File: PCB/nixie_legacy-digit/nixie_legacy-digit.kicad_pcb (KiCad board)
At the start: 2 copper layers, 50.8 x 78.7 mm, 11 parts

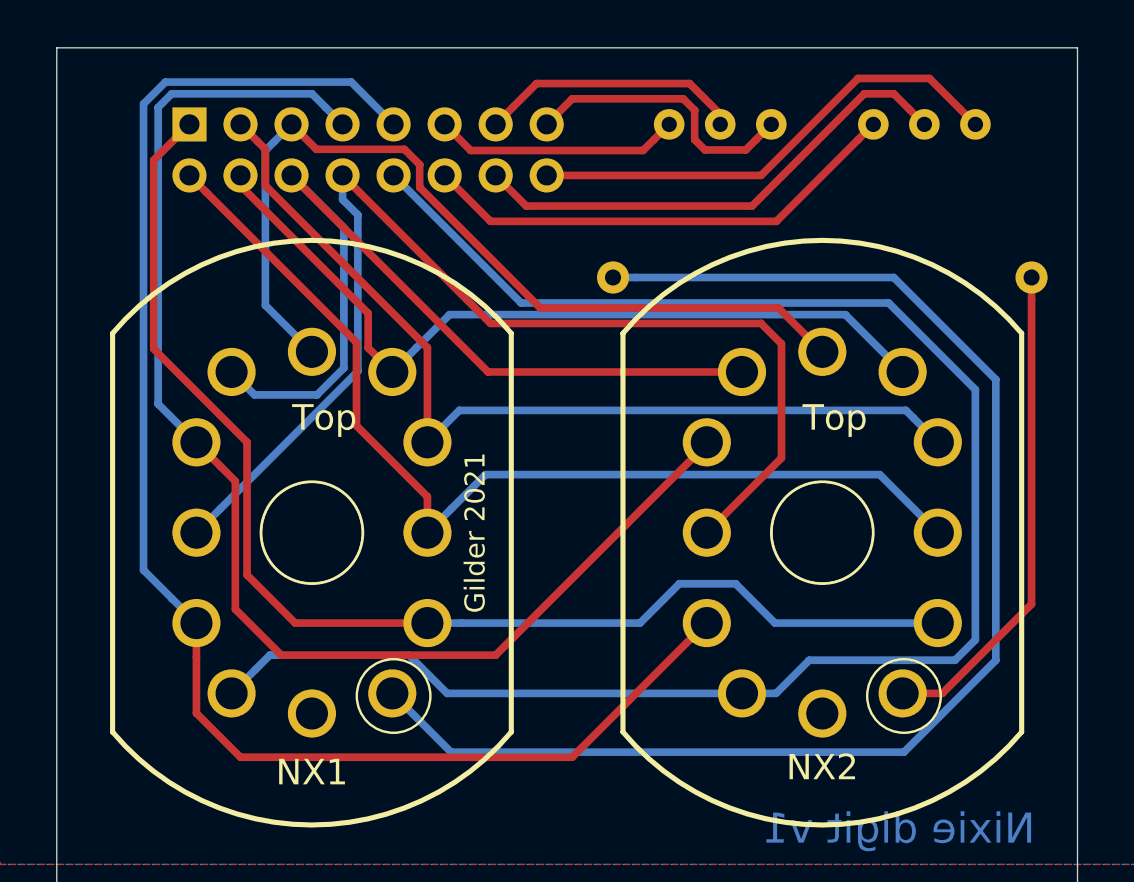
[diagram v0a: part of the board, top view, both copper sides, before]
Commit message: digit pcb updated. added breakout for left decimal point (for 4-digit clocks)
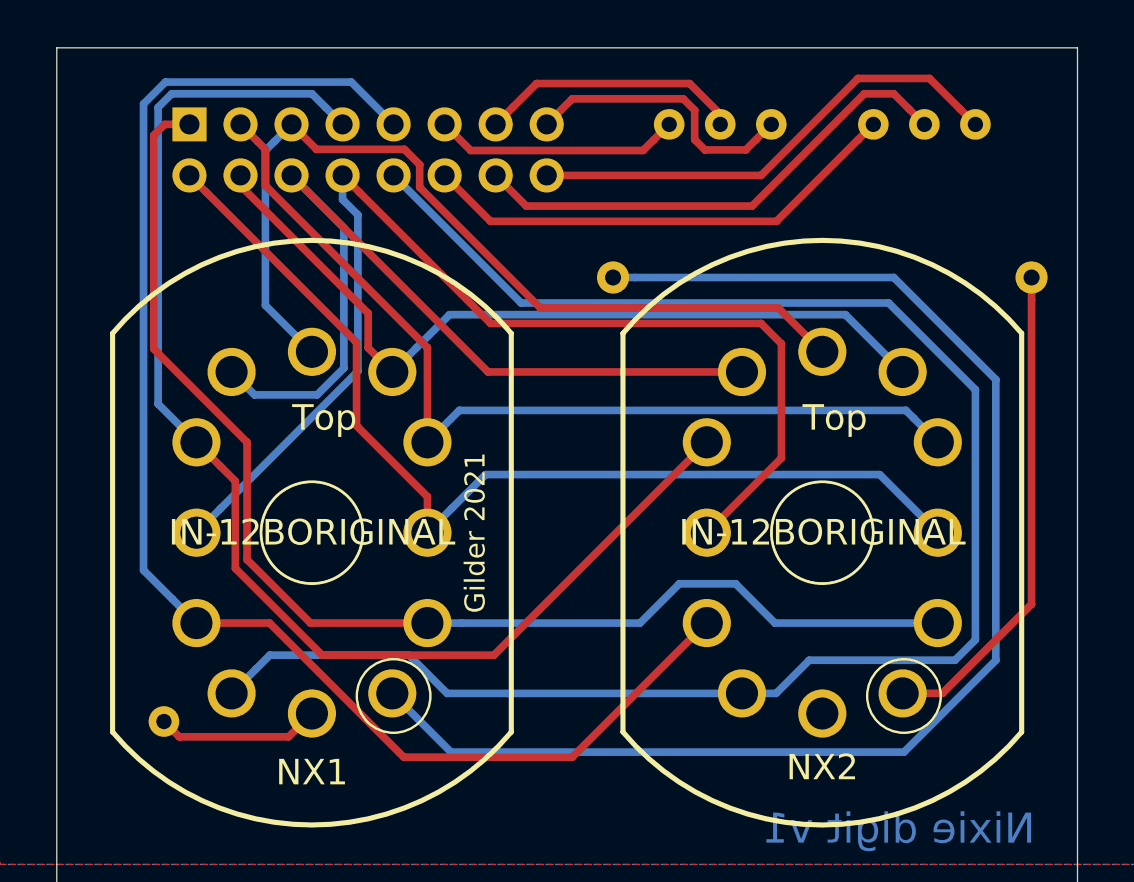
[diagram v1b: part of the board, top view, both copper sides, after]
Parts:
- added dp: HEADER_1, customPartsLibrary:Single_pad-1x1, F.Cu at (81.5, 118.6)
- J1: renamed from Affix header this side (rear)
- NX1, NX2: value (none) -> IN-12BORIGINAL
- renumbered Left-20k to R1, Right-20k to R2
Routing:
- net Net-(NX1-PadLHDP): track 0.00 -> 8.16 mm
- net 2: track 74.3 -> 71.6 mm
- net 4: track 65.5 -> 64.3 mm
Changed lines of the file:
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@@
     (thickness 1.6)
     (drawings 23)
-    (tracks 149)
+    (tracks 151)
     (zones 0)
-    (modules 11)
+    (modules 12)
     (nets 21)
   )
@@
     (35 F.Paste user)
     (36 B.SilkS user)
-    (37 F.SilkS user)
+    (37 F.SilkS user hide)
     (38 B.Mask user)
     (39 F.Mask user)
@@
   )
   (setup
-    (last_trace_width 0.25)
+    (last_trace_width 0.381)
     (user_trace_width 0.381)
     (trace_clearance 0.2)
@@
     (add_net digit6lsb)
   )
+  (module customPartsLibrary:Single_pad-1x1 (layer F.Cu)
+    (at 81.534 118.618)
+    (fp_text reference dp (at -1.016 -1.778) (layer B.SilkS)
+      (effects (font (size 1 1) (thickness 0.15)) (justify mirror))
+    )
+    (fp_text value HEADER_1 (at 0 2.286) (layer F.Fab)
+      (effects (font (size 1 1) (thickness 0.15)))
+    )
+    (pad 1 thru_hole circle (at 0 0) (size 1.524 1.524) (drill 0.762) (layers *.Cu *.Mask)
+      (net 17 "Net-(NX1-PadLHDP)"))
+  )
   (module Resistor_THT:R_Axial_DIN0207_L6.3mm_D2.5mm_P7.62mm_Horizontal (layer B.Cu)
     (at 124.714 88.9 270)
     (descr "Resistor, Axial_DIN0207 series, Axial, Horizontal, pin pitch=7.62mm, 0.25W = 1/4W, length*diameter=6.3*2.5mm^2, http://cdn-reichelt.de/documents/datenblatt/B400/1_4W%23YAG.pdf")
     (tags "Resistor Axial_DIN0207 series Axial Horizontal pin pitch 7.62mm 0.25W = 1/4W length 6.3mm diameter 2.5mm")
-    (fp_text reference Right-20k (at 2.794 0 90) (layer B.SilkS)
+    (fp_text reference R2 (at 2.794 0 90) (layer B.SilkS)
       (effects (font (size 1 1) (thickness 0.15)) (justify mirror))
     )
@@
     (descr "Resistor, Axial_DIN0207 series, Axial, Horizontal, pin pitch=7.62mm, 0.25W = 1/4W, length*diameter=6.3*2.5mm^2, http://cdn-reichelt.de/documents/datenblatt/B400/1_4W%23YAG.pdf")
     (tags "Resistor Axial_DIN0207 series Axial Horizontal pin pitch 7.62mm 0.25W = 1/4W length 6.3mm diameter 2.5mm")
-    (fp_text reference Left-20k (at 3.302 0 270) (layer B.SilkS)
+    (fp_text reference R1 (at 3.302 0 270) (layer B.SilkS)
       (effects (font (size 1 1) (thickness 0.15)) (justify mirror))
     )
@@
       (effects (font (size 1.27 1.27) (thickness 0.1016)))
     )
-    (fp_text value " " (at 0 0) (layer F.SilkS)
+    (fp_text value IN-12BORIGINAL (at 0 0) (layer F.SilkS)
       (effects (font (size 1.27 1.27) (thickness 0.15)))
     )
@@
       (effects (font (size 1.27 1.27) (thickness 0.1016)))
     )
-    (fp_text value " " (at 0 0) (layer F.SilkS)
+    (fp_text value IN-12BORIGINAL (at 0 0) (layer F.SilkS)
       (effects (font (size 1.27 1.27) (thickness 0.15)))
     )
@@
     (descr "Through hole straight pin header, 2x08, 2.54mm pitch, double rows")
     (tags "Through hole pin header THT 2x08 2.54mm double row")
-    (fp_text reference "Affix header this side (rear)" (at -2.032 -8.128) (layer B.SilkS)
+    (fp_text reference J1 (at -2.032 -8.128) (layer B.SilkS)
       (effects (font (size 1 1) (thickness 0.15)) (justify mirror))
     )
@@
   (segment (start 121.92 114.554) (end 121.92 102.108) (width 0.381) (layer B.Cu) (net 7))
   (segment (start 121.92 102.108) (end 117.602 97.79) (width 0.381) (layer B.Cu) (net 7))
-  (segment (start 83.15198 115.413812) (end 83.15198 113.71834) (width 0.381) (layer F.Cu) (net 8))
-  (segment (start 83.15198 118.20398) (end 83.15198 115.413812) (width 0.381) (layer F.Cu) (net 8))
-  (segment (start 85.344 120.396) (end 83.15198 118.20398) (width 0.381) (layer F.Cu) (net 8))
-  (segment (start 101.854 120.396) (end 85.344 120.396) (width 0.381) (layer F.Cu) (net 8))
-  (segment (start 108.55198 113.71834) (end 108.53166 113.71834) (width 0.381) (layer F.Cu) (net 8))
-  (segment (start 108.53166 113.71834) (end 101.854 120.396) (width 0.381) (layer F.Cu) (net 8))
   (segment (start 80.518 111.08436) (end 81.953101 112.519461) (width 0.381) (layer B.Cu) (net 8))
   (segment (start 81.953101 112.519461) (end 83.15198 113.71834) (width 0.381) (layer B.Cu) (net 8))
@@
   (segment (start 90.858989 86.794989) (end 81.607011 86.794989) (width 0.381) (layer B.Cu) (net 8))
   (segment (start 92.964 88.9) (end 90.858989 86.794989) (width 0.381) (layer B.Cu) (net 8))
+  (segment (start 86.79434 113.71834) (end 83.15198 113.71834) (width 0.381) (layer F.Cu) (net 8))
+  (segment (start 93.472 120.396) (end 86.79434 113.71834) (width 0.381) (layer F.Cu) (net 8))
+  (segment (start 101.854 120.396) (end 93.472 120.396) (width 0.381) (layer F.Cu) (net 8))
+  (segment (start 108.55198 113.71834) (end 108.53166 113.71834) (width 0.381) (layer F.Cu) (net 8))
+  (segment (start 108.53166 113.71834) (end 101.854 120.396) (width 0.381) (layer F.Cu) (net 8))
   (segment (start 91.273999 92.289999) (end 90.424 91.44) (width 0.381) (layer F.Cu) (net 9))
   (segment (start 97.79 98.806) (end 91.273999 92.289999) (width 0.381) (layer F.Cu) (net 9))
@@
   (segment (start 91.186 101.18598) (end 84.350859 108.021121) (width 0.381) (layer B.Cu) (net 9))
   (segment (start 84.350859 108.021121) (end 83.15198 109.22) (width 0.381) (layer B.Cu) (net 9))
-  (segment (start 85.09 106.65968) (end 84.350859 105.920539) (width 0.381) (layer F.Cu) (net 10))
-  (segment (start 85.09 113.03) (end 85.09 106.65968) (width 0.381) (layer F.Cu) (net 10))
-  (segment (start 87.376 115.316) (end 85.09 113.03) (width 0.381) (layer F.Cu) (net 10))
-  (segment (start 98.044 115.316) (end 87.376 115.316) (width 0.381) (layer F.Cu) (net 10))
-  (segment (start 108.55198 104.80802) (end 98.044 115.316) (width 0.381) (layer F.Cu) (net 10))
-  (segment (start 108.55198 104.72166) (end 108.55198 104.80802) (width 0.381) (layer F.Cu) (net 10))
-  (segment (start 84.350859 105.920539) (end 83.15198 104.72166) (width 0.381) (layer F.Cu) (net 10))
   (segment (start 89.574001 88.050001) (end 90.424 88.9) (width 0.381) (layer B.Cu) (net 10))
   (segment (start 88.9 87.376) (end 89.574001 88.050001) (width 0.381) (layer B.Cu) (net 10))
@@
   (segment (start 81.925098 87.376) (end 88.9 87.376) (width 0.381) (layer B.Cu) (net 10))
   (segment (start 81.244489 102.814169) (end 81.244489 88.056609) (width 0.381) (layer B.Cu) (net 10))
+  (segment (start 84.350859 105.920539) (end 83.15198 104.72166) (width 0.381) (layer F.Cu) (net 10))
+  (segment (start 85.09 106.65968) (end 84.350859 105.920539) (width 0.381) (layer F.Cu) (net 10))
+  (segment (start 85.09 110.998) (end 85.09 106.65968) (width 0.381) (layer F.Cu) (net 10))
+  (segment (start 89.408 115.316) (end 85.09 110.998) (width 0.381) (layer F.Cu) (net 10))
+  (segment (start 108.55198 104.72166) (end 97.95764 115.316) (width 0.381) (layer F.Cu) (net 10))
+  (segment (start 97.95764 115.316) (end 89.408 115.316) (width 0.381) (layer F.Cu) (net 10))
   (segment (start 97.66554 101.22154) (end 87.884 91.44) (width 0.381) (layer F.Cu) (net 11))
   (segment (start 110.30204 101.22154) (end 97.66554 101.22154) (width 0.381) (layer F.Cu) (net 11))
@@
   (segment (start 94.64802 107.431896) (end 91.118071 103.901947) (width 0.381) (layer F.Cu) (net 15))
   (segment (start 94.64802 109.22) (end 94.64802 107.431896) (width 0.381) (layer F.Cu) (net 15))
-  (segment (start 81.026 90.678) (end 82.804 88.9) (width 0.381) (layer F.Cu) (net 16))
-  (segment (start 81.026 100.076) (end 81.026 90.678) (width 0.381) (layer F.Cu) (net 16))
-  (segment (start 85.671011 104.721011) (end 81.026 100.076) (width 0.381) (layer F.Cu) (net 16))
-  (segment (start 85.671011 111.325011) (end 85.671011 104.721011) (width 0.381) (layer F.Cu) (net 16))
-  (segment (start 94.64802 113.71834) (end 88.06434 113.71834) (width 0.381) (layer F.Cu) (net 16))
-  (segment (start 88.06434 113.71834) (end 85.671011 111.325011) (width 0.381) (layer F.Cu) (net 16))
   (segment (start 96.343492 113.71834) (end 94.64802 113.71834) (width 0.381) (layer B.Cu) (net 16))
   (segment (start 105.22966 113.71834) (end 96.343492 113.71834) (width 0.381) (layer B.Cu) (net 16))
@@
   (segment (start 120.04802 113.71834) (end 111.94034 113.71834) (width 0.381) (layer B.Cu) (net 16))
   (segment (start 111.94034 113.71834) (end 109.982 111.76) (width 0.381) (layer B.Cu) (net 16))
+  (segment (start 88.82634 113.71834) (end 85.671011 110.563011) (width 0.381) (layer F.Cu) (net 16))
+  (segment (start 94.64802 113.71834) (end 88.82634 113.71834) (width 0.381) (layer F.Cu) (net 16))
+  (segment (start 85.671011 110.563011) (end 85.671011 104.721011) (width 0.381) (layer F.Cu) (net 16))
+  (segment (start 81.573 88.9) (end 82.804 88.9) (width 0.381) (layer F.Cu) (net 16))
+  (segment (start 85.671011 104.721011) (end 81.026 100.076) (width 0.381) (layer F.Cu) (net 16))
+  (segment (start 81.026 100.076) (end 81.026 89.447) (width 0.381) (layer F.Cu) (net 16))
+  (segment (start 81.026 89.447) (end 81.573 88.9) (width 0.381) (layer F.Cu) (net 16))
+  (segment (start 82.295999 119.379999) (end 81.534 118.618) (width 0.381) (layer F.Cu) (net 17))
+  (segment (start 88.9 118.21922) (end 87.739221 119.379999) (width 0.381) (layer F.Cu) (net 17))
+  (segment (start 87.739221 119.379999) (end 82.295999 119.379999) (width 0.381) (layer F.Cu) (net 17))
   (segment (start 105.01737 96.52) (end 103.886 96.52) (width 0.381) (layer B.Cu) (net 18))
   (segment (start 95.8215 120.142) (end 118.364 120.142) (width 0.381) (layer B.Cu) (net 18))

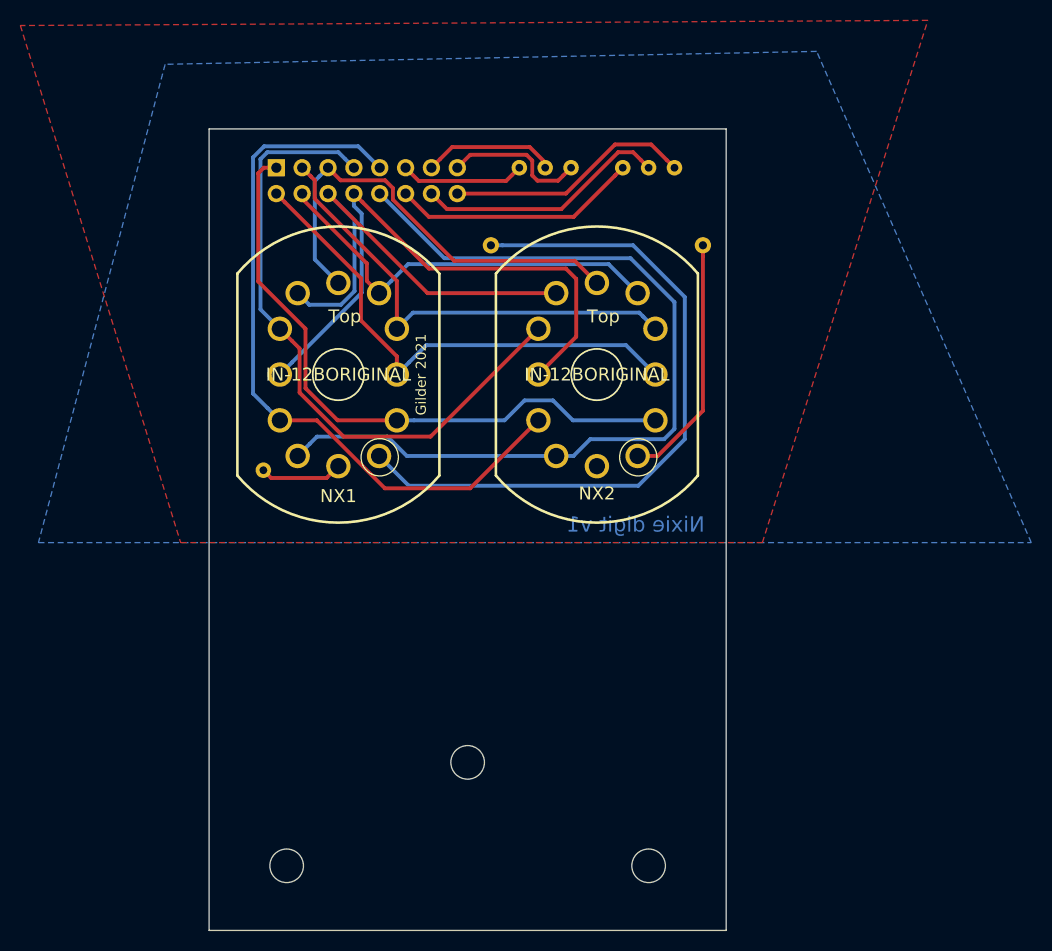
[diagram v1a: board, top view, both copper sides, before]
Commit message: digit pcb update. removed flood fill copper
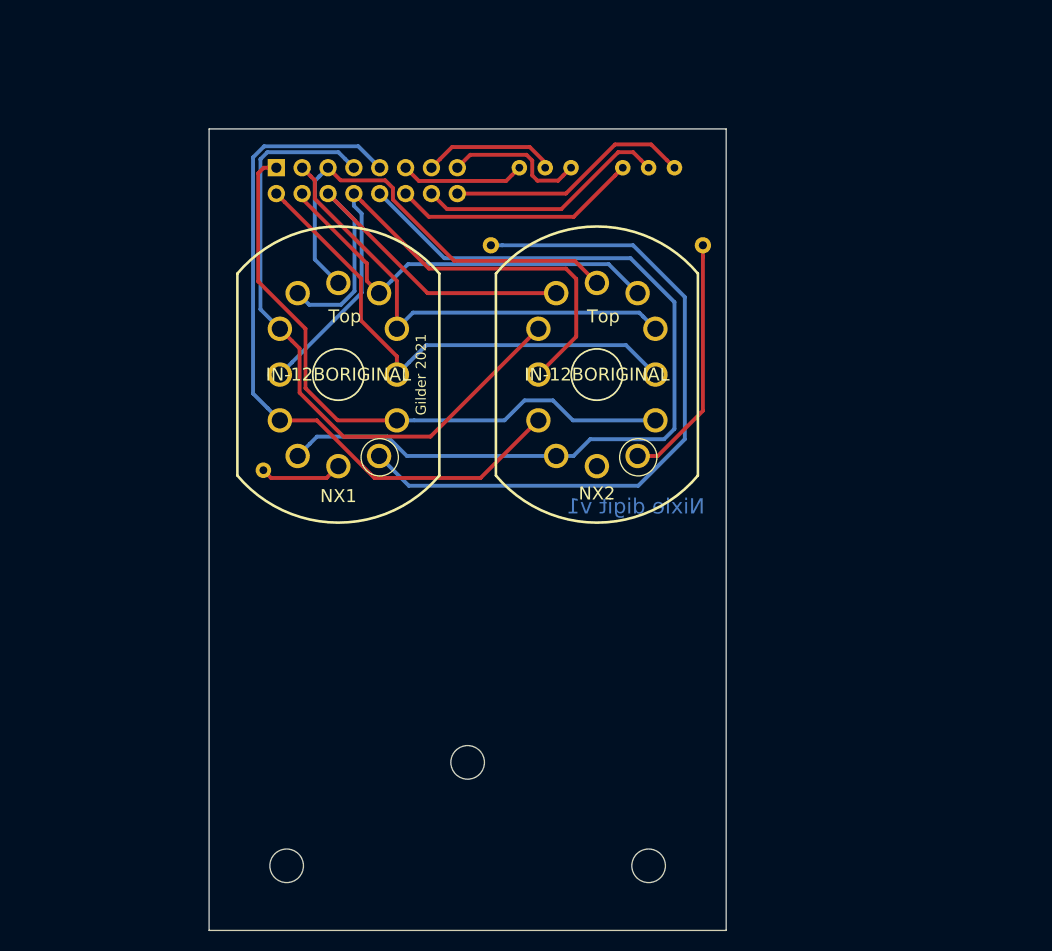
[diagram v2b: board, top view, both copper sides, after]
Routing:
- net 2: track 71.6 -> 70.8 mm
- removed copper zone on B.Cu, net (none)
- removed copper zone on F.Cu, net (none)
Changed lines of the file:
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@@
     (effects (font (size 1 1) (thickness 0.15)))
   )
-  (gr_line (start 86.36 130.302) (end 85.09 129.032) (layer B.SilkS) (width 0.12))
-  (gr_line (start 87.63 129.032) (end 86.36 130.302) (layer B.SilkS) (width 0.12))
-  (gr_line (start 86.36 127) (end 86.36 130.302) (layer B.SilkS) (width 0.12))
-  (gr_line (start 116.84 130.302) (end 115.57 129.032) (layer B.SilkS) (width 0.12))
-  (gr_line (start 118.11 129.032) (end 116.84 130.302) (layer B.SilkS) (width 0.12))
-  (gr_line (start 116.84 127) (end 116.84 130.302) (layer B.SilkS) (width 0.12))
-  (gr_text "Safe to cut & drill" (at 101.6 130.302) (layer B.SilkS)
+  (gr_line (start 86.36 129.032) (end 85.09 127.762) (layer B.SilkS) (width 0.12))
+  (gr_line (start 87.63 127.762) (end 86.36 129.032) (layer B.SilkS) (width 0.12))
+  (gr_line (start 86.36 125.73) (end 86.36 129.032) (layer B.SilkS) (width 0.12))
+  (gr_line (start 116.84 129.032) (end 115.57 127.762) (layer B.SilkS) (width 0.12))
+  (gr_line (start 118.11 127.762) (end 116.84 129.032) (layer B.SilkS) (width 0.12))
+  (gr_line (start 116.84 125.73) (end 116.84 129.032) (layer B.SilkS) (width 0.12))
+  (gr_text "Safe to cut & drill" (at 101.6 129.032) (layer B.SilkS)
     (effects (font (size 1 1) (thickness 0.15)) (justify mirror))
   )
-  (gr_line (start 127 125.73) (end 76.2 125.73) (layer B.SilkS) (width 0.12))
+  (gr_line (start 127 124.46) (end 76.2 124.46) (layer B.SilkS) (width 0.12))
   (gr_text "WARNING: High Voltage" (at 91.694 94.488) (layer B.SilkS)
     (effects (font (size 1 1) (thickness 0.15)) (justify mirror))
   )
-  (gr_text "Nixie digit v1" (at 118.11 123.952) (layer B.Cu)
+  (gr_text "Nixie digit v1" (at 118.11 122.174) (layer B.Cu)
     (effects (font (size 1.5 1.5) (thickness 0.3)) (justify mirror))
   )
@@
   (segment (start 92.964 88.9) (end 90.858989 86.794989) (width 0.381) (layer B.Cu) (net 8))
   (segment (start 86.79434 113.71834) (end 83.15198 113.71834) (width 0.381) (layer F.Cu) (net 8))
-  (segment (start 93.472 120.396) (end 86.79434 113.71834) (width 0.381) (layer F.Cu) (net 8))
-  (segment (start 101.854 120.396) (end 93.472 120.396) (width 0.381) (layer F.Cu) (net 8))
+  (segment (start 92.456 119.38) (end 86.79434 113.71834) (width 0.381) (layer F.Cu) (net 8))
+  (segment (start 102.87 119.38) (end 92.456 119.38) (width 0.381) (layer F.Cu) (net 8))
   (segment (start 108.55198 113.71834) (end 108.53166 113.71834) (width 0.381) (layer F.Cu) (net 8))
-  (segment (start 108.53166 113.71834) (end 101.854 120.396) (width 0.381) (layer F.Cu) (net 8))
+  (segment (start 108.53166 113.71834) (end 102.87 119.38) (width 0.381) (layer F.Cu) (net 8))
   (segment (start 91.273999 92.289999) (end 90.424 91.44) (width 0.381) (layer F.Cu) (net 9))
   (segment (start 97.79 98.806) (end 91.273999 92.289999) (width 0.381) (layer F.Cu) (net 9))
@@
   (segment (start 118.29796 117.21846) (end 120.27154 117.21846) (width 0.381) (layer F.Cu) (net 20))
   (segment (start 120.27154 117.21846) (end 124.714 112.776) (width 0.381) (layer F.Cu) (net 20))
-  (zone (net 0) (net_name "") (layer B.Cu) (hatch edge 0.508)
-    (connect_pads (clearance 0.508))
-    (min_thickness 0.254)
-    (fill yes (arc_segments 32) (thermal_gap 0.508) (thermal_bridge_width 0.508))
-    (polygon
-      (pts
-        (xy 71.882 78.74) (xy 59.436 125.73) (xy 156.972 125.73) (xy 135.89 77.47)
-      )
-    )
-  )
-  (zone (net 0) (net_name "") (layer F.Cu) (hatch edge 0.508)
-    (connect_pads (clearance 0.508))
-    (min_thickness 0.254)
-    (fill yes (arc_segments 32) (thermal_gap 0.508) (thermal_bridge_width 0.508))
-    (polygon
-      (pts
-        (xy 146.812 74.422) (xy 57.658 74.93) (xy 73.406 125.73) (xy 130.556 125.73)
-      )
-    )
-  )
 )
